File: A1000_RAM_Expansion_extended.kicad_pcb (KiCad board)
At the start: 2 copper layers, 149.5 x 51.6 mm, 37 parts, among them J1 Front_Connector, J2 Conn_02x05, U1 XC9572XL-xxVQx64, U2 LD1117S33TR_SOT223

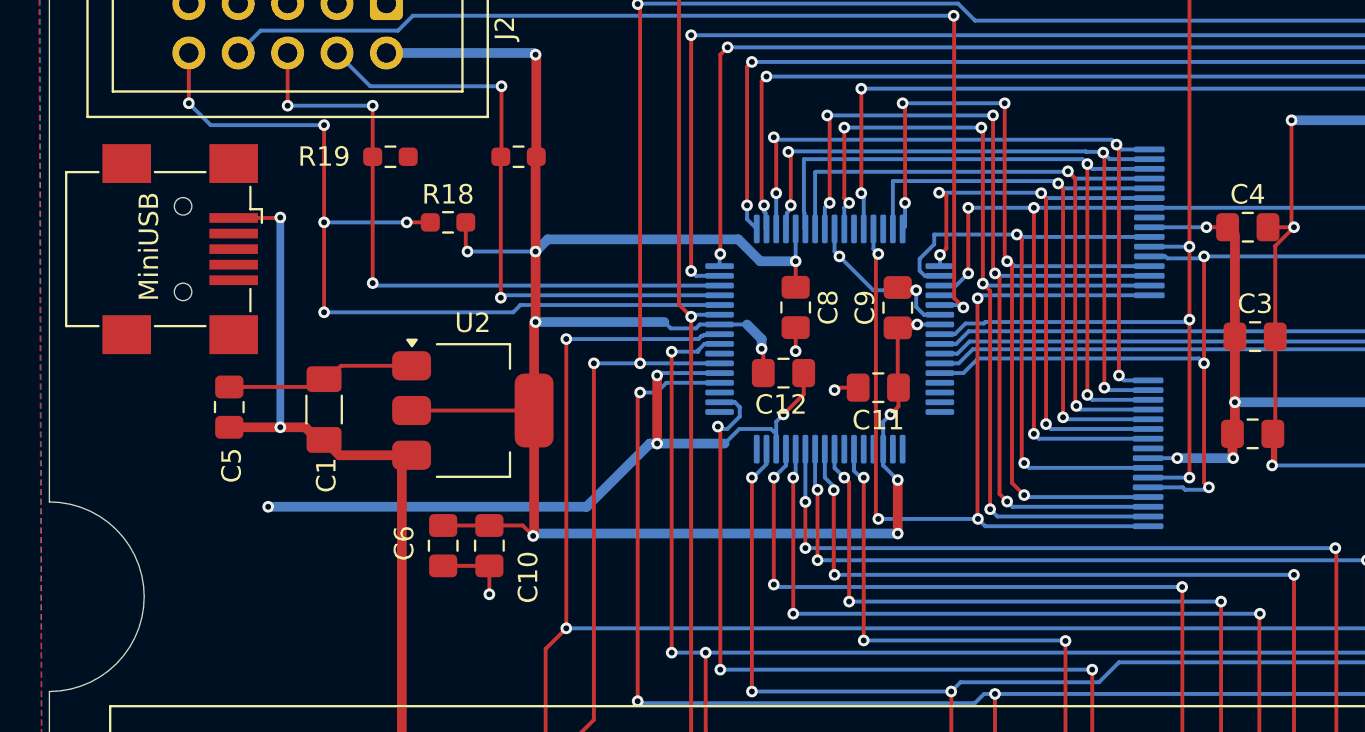
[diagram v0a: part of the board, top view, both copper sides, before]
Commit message: Planes revised, gitignore
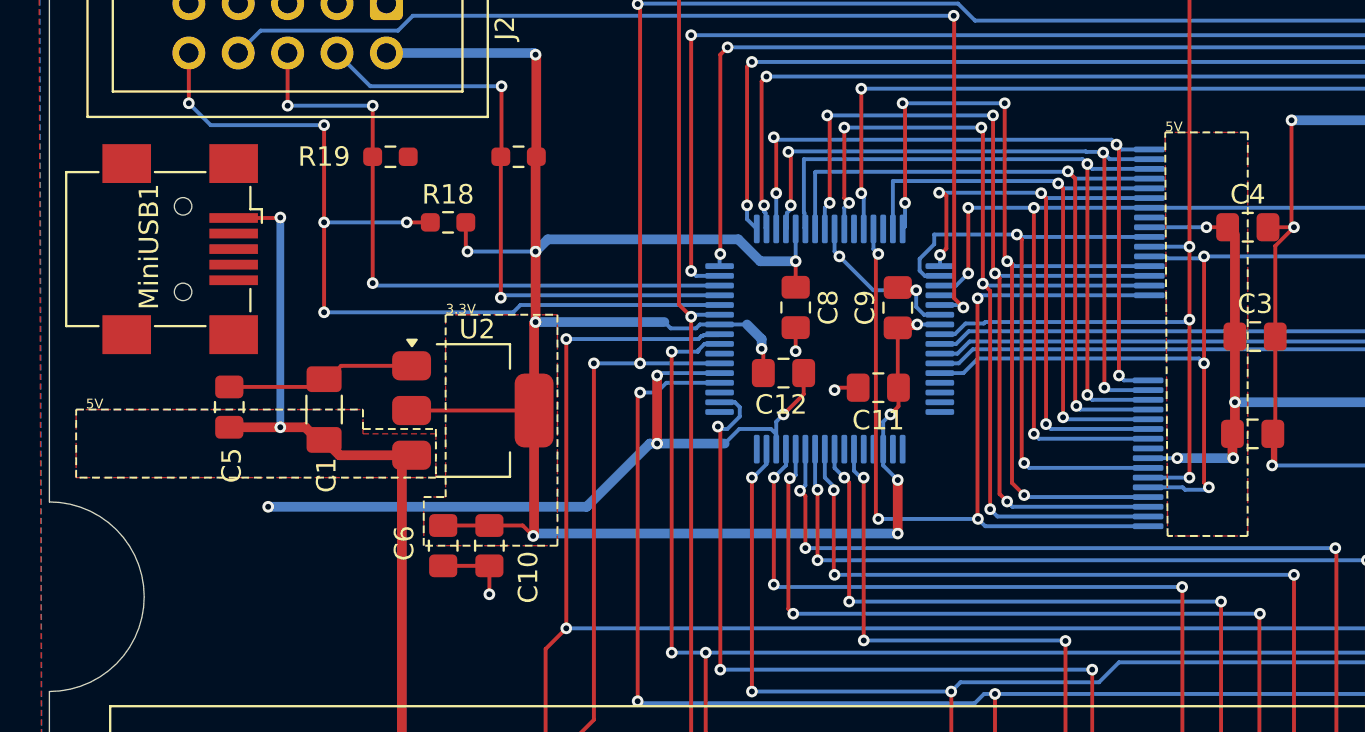
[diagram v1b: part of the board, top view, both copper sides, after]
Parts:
- J2: value Conn_02x05 -> Conn_02x05_Odd_Even
- renumbered MiniUSB to MiniUSB1
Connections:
- MiniUSB1 pad 2: (no net) -> unconnected-(MiniUSB1-D--Pad2)
- MiniUSB1 pad 3: (no net) -> unconnected-(MiniUSB1-D+-Pad3)
- MiniUSB1 pad 4: (no net) -> unconnected-(MiniUSB1-ID-Pad4)
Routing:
- added copper zone on F.Cu, net +3.3V
- added copper zone on F.Cu, net +5V
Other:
- board text added: "3.3V"
- board text added: "5V"

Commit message: In da Zone..
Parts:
- added +5V: TestPoint_Pad_D2.0mm, TestPoint:TestPoint_Pad_D2.0mm, B.Cu at (77.5, 84.5)
- added GND: TestPoint_Pad_D2.0mm, TestPoint:TestPoint_Pad_D2.0mm, B.Cu at (77.5, 88.8)
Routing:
- net GND: track 155.5 -> 175.6 mm, vias 16 -> 18
- net +3.3V: track 113.2 -> 106.9 mm, vias 11 -> 34
- net +5V: track 236.0 -> 238.0 mm, vias 9 -> 10
- added copper zone on B.Cu, net +3.3V
- added copper zone on B.Cu, net +5V
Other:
- board text added: "100nF"
- board text added: "10uF"
- board text added: "C2"

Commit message: Cleanup
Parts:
- removed +5V, GND: TestPoint_Pad_D2.0mm, TestPoint:TestPoint_Pad_D2.0mm
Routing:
- net GND: track 175.6 -> 164.5 mm
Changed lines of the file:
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@@
 		(embedded_fonts no)
 	)
-	(footprint "TestPoint:TestPoint_Pad_D2.0mm"
-		(layer "B.Cu")
-		(at 77.5 88.75 180)
-		(descr "SMD pad as test Point, diameter 2.0mm")
-		(tags "test point SMD pad")
-		(property "Reference" "GND"
-			(at 0 -3.5 90)
-			(layer "B.SilkS")
-			(effects
-				(font
-					(size 1 1)
-					(thickness 0.15)
-				)
-				(justify mirror)
-			)
-		)
-		(property "Value" "TestPoint_Pad_D2.0mm"
-			(at 0 -2.05 0)
-			(layer "B.Fab")
-			(effects
-				(font
-					(size 1 1)
-					(thickness 0.15)
-				)
-				(justify mirror)
-			)
-		)
-		(property "Datasheet" ""
-			(at 0 0 0)
-			(unlocked yes)
-			(layer "B.Fab")
-			(hide yes)
-			(effects
-				(font
-					(size 1.27 1.27)
-					(thickness 0.15)
-				)
-				(justify mirror)
-			)
-		)
-		(property "Description" ""
-			(at 0 0 0)
-			(unlocked yes)
-			(layer "B.Fab")
-			(hide yes)
-			(effects
-				(font
-					(size 1.27 1.27)
-					(thickness 0.15)
-				)
-				(justify mirror)
-			)
-		)
-		(attr exclude_from_pos_files exclude_from_bom)
-		(fp_circle
-			(center 0 0)
-			(end 0 -1.2)
-			(stroke
-				(width 0.12)
-				(type solid)
-			)
-			(fill no)
-			(layer "B.SilkS")
-		)
-		(fp_circle
-			(center 0 0)
-			(end 1.5 0)
-			(stroke
-				(width 0.05)
-				(type solid)
-			)
-			(fill no)
-			(layer "B.CrtYd")
-		)
-		(fp_text user "${REFERENCE}"
-			(at 0 2 0)
-			(layer "B.Fab")
-			(effects
-				(font
-					(size 1 1)
-					(thickness 0.15)
-				)
-				(justify mirror)
-			)
-		)
-		(pad "1" smd circle
-			(at 0 0 180)
-			(size 2 2)
-			(layers "F.Cu" "B.Mask")
-		)
-		(embedded_fonts no)
-	)
 	(footprint "Resistor_SMD:R_Array_Convex_4x0603"
 		(layer "B.Cu")
@@
 		(embedded_fonts no)
 	)
-	(footprint "TestPoint:TestPoint_Pad_D2.0mm"
-		(layer "B.Cu")
-		(at 77.5 84.5 180)
-		(descr "SMD pad as test Point, diameter 2.0mm")
-		(tags "test point SMD pad")
-		(property "Reference" "+5V"
-			(at 0 3.5 90)
-			(layer "B.SilkS")
-			(effects
-				(font
-					(size 1 1)
-					(thickness 0.15)
-				)
-				(justify mirror)
-			)
-		)
-		(property "Value" "TestPoint_Pad_D2.0mm"
-			(at 0 -2.05 0)
-			(layer "B.Fab")
-			(effects
-				(font
-					(size 1 1)
-					(thickness 0.15)
-				)
-				(justify mirror)
-			)
-		)
-		(property "Datasheet" ""
-			(at 0 0 0)
-			(unlocked yes)
-			(layer "B.Fab")
-			(hide yes)
-			(effects
-				(font
-					(size 1.27 1.27)
-					(thickness 0.15)
-				)
-				(justify mirror)
-			)
-		)
-		(property "Description" ""
-			(at 0 0 0)
-			(unlocked yes)
-			(layer "B.Fab")
-			(hide yes)
-			(effects
-				(font
-					(size 1.27 1.27)
-					(thickness 0.15)
-				)
-				(justify mirror)
-			)
-		)
-		(attr exclude_from_pos_files exclude_from_bom)
-		(fp_circle
-			(center 0 0)
-			(end 0 -1.2)
-			(stroke
-				(width 0.12)
-				(type solid)
-			)
-			(fill no)
-			(layer "B.SilkS")
-		)
-		(fp_circle
-			(center 0 0)
-			(end 1.5 0)
-			(stroke
-				(width 0.05)
-				(type solid)
-			)
-			(fill no)
-			(layer "B.CrtYd")
-		)
-		(fp_text user "${REFERENCE}"
-			(at 0 2 0)
-			(layer "B.Fab")
-			(effects
-				(font
-					(size 1 1)
-					(thickness 0.15)
-				)
-				(justify mirror)
-			)
-		)
-		(pad "1" smd circle
-			(at 0 0 180)
-			(size 2 2)
-			(layers "F.Cu" "B.Mask")
-		)
-		(embedded_fonts no)
-	)
 	(footprint "Package_SO:TSOP-I-32_18.4x8mm_P0.5mm"
 		(layer "B.Cu")
@@
 		(start 80.375 81.5875)
 		(end 84.85 81.5875)
-		(width 0.2)
+		(width 0.5)
 		(layer "F.Cu")
 		(net 73)
@@
 	)
 	(via
-		(at 122 61)
+		(at 128.125 61)
 		(size 0.6)
 		(drill 0.3)
@@
 	)
 	(via blind
-		(at 82.375 87.75)
+		(at 87.375 87.75)
 		(size 0.6)
 		(drill 0.3)
@@
 	)
 	(segment
-		(start 98.75 87.75)
-		(end 82.375 87.75)
-		(width 0.5)
-		(layer "B.Cu")
-		(net 73)
-	)
-	(segment
-		(start 102 84.5)
-		(end 98.75 87.75)
-		(width 0.5)
-		(layer "B.Cu")
-		(net 73)
-	)
-	(segment
 		(start 108.5 84.016176)
 		(end 108.232824 83.749)
@@
 	)
 	(segment
+		(start 102 84.5)
+		(end 102.375 84.5)
+		(width 0.5)
+		(layer "B.Cu")
+		(net 73)
+	)
+	(segment
 		(start 105.5875 80.875)
 		(end 102.5 80.875)
@@
 	)
 	(segment
+		(start 135.125 61)
+		(end 128.125 61)
+		(width 0.5)
+		(layer "B.Cu")
+		(net 73)
+	)
+	(segment
+		(start 98.75 87.75)
+		(end 102 84.5)
+		(width 0.5)
+		(layer "B.Cu")
+		(net 73)
+	)
+	(segment
 		(start 111.5 73.4625)
 		(end 111.5 74.625)
@@
 	)
 	(segment
-		(start 102.375 84.5)
-		(end 102 84.5)
+		(start 87.375 87.75)
+		(end 98.75 87.75)
 		(width 0.5)
 		(layer "B.Cu")
@@
 	)
 	(segment
-		(start 135.125 61)
-		(end 122 61)
-		(width 0.5)
-		(layer "B.Cu")
-		(net 73)
-	)
-	(segment
 		(start 134 85.625)
 		(end 141.25 85.625)
@@
 	)
 	(zone
-		(net 75)
-		(net_name "+5V")
-		(layer "F.Cu")
-		(hatch edge 0.5)
-		(priority 4)
-		(connect_pads yes
-			(clearance 0.5)
-		)
-		(min_thickness 0.25)
-		(filled_areas_thickness no)
-		(fill yes
-			(thermal_gap 0.5)
-			(thermal_bridge_width 0.5)
-		)
-		(polygon
-			(pts
-				(xy 72.5 82.75) (xy 87.25 82.75) (xy 87.25 84) (xy 91 84) (xy 91 86.25) (xy 72.5 86.25)
-			)
-		)
-	)
-	(zone
 		(net 1)
 		(net_name "+3.3V")
@@
 	)
 	(zone
+		(net 75)
+		(net_name "+5V")
+		(layer "F.Cu")
+		(hatch edge 0.5)
+		(priority 4)
+		(connect_pads yes
+			(clearance 0.5)
+		)
+		(min_thickness 0.25)
+		(filled_areas_thickness no)
+		(fill yes
+			(thermal_gap 0.5)
+			(thermal_bridge_width 0.5)
+		)
+		(polygon
+			(pts
+				(xy 72.5 82.75) (xy 87.25 82.75) (xy 87.25 84) (xy 91 84) (xy 91 86.25) (xy 72.5 86.25)
+			)
+		)
+	)
+	(zone
 		(net 1)
 		(net_name "+3.3V")
@@
 	)
 	(zone
-		(net 75)
-		(net_name "+5V")
-		(layer "B.Cu")
-		(hatch edge 0.5)
-		(priority 6)
-		(connect_pads
-			(clearance 0.5)
-		)
-		(min_thickness 0.25)
-		(filled_areas_thickness no)
-		(fill yes
-			(thermal_gap 0.5)
-			(thermal_bridge_width 0.5)
-		)
-		(polygon
-			(pts
-				(xy 128.5 68.5) (xy 132.75 68.5) (xy 132.75 89.25) (xy 128.625 89.25)
-			)
-		)
-	)
-	(zone
 		(net 1)
 		(net_name "+3.3V")
@@
 			)
 		)
+	)
+	(zone
+		(net 75)
+		(net_name "+5V")
+		(layer "B.Cu")
+		(hatch edge 0.5)
+		(priority 6)
+		(connect_pads
+			(clearance 0.5)
+		)
+		(min_thickness 0.25)
+		(filled_areas_thickness no)
+		(fill yes
+			(thermal_gap 0.5)
+			(thermal_bridge_width 0.5)
+		)
+		(polygon
+			(pts
+				(xy 128.5 68.5) (xy 132.75 68.5) (xy 132.75 89.25) (xy 128.625 89.25)
+			)
+		)

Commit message: Cleanup
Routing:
- net +3.3V: track 106.9 -> 95.9 mm
- net +5V: track 238.0 -> 228.4 mm
- net GND: track 164.5 -> 162.1 mm
